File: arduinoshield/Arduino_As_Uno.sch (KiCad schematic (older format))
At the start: 25 parts, among them J1 Conn_01x08, P1 Power, P2 Analog, P3 Digital, P4 Digital, P5 CONN_01X01, P6 CONN_01X01, P7 CONN_01X01, P8 CONN_01X01, U1 MC7815ACTG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

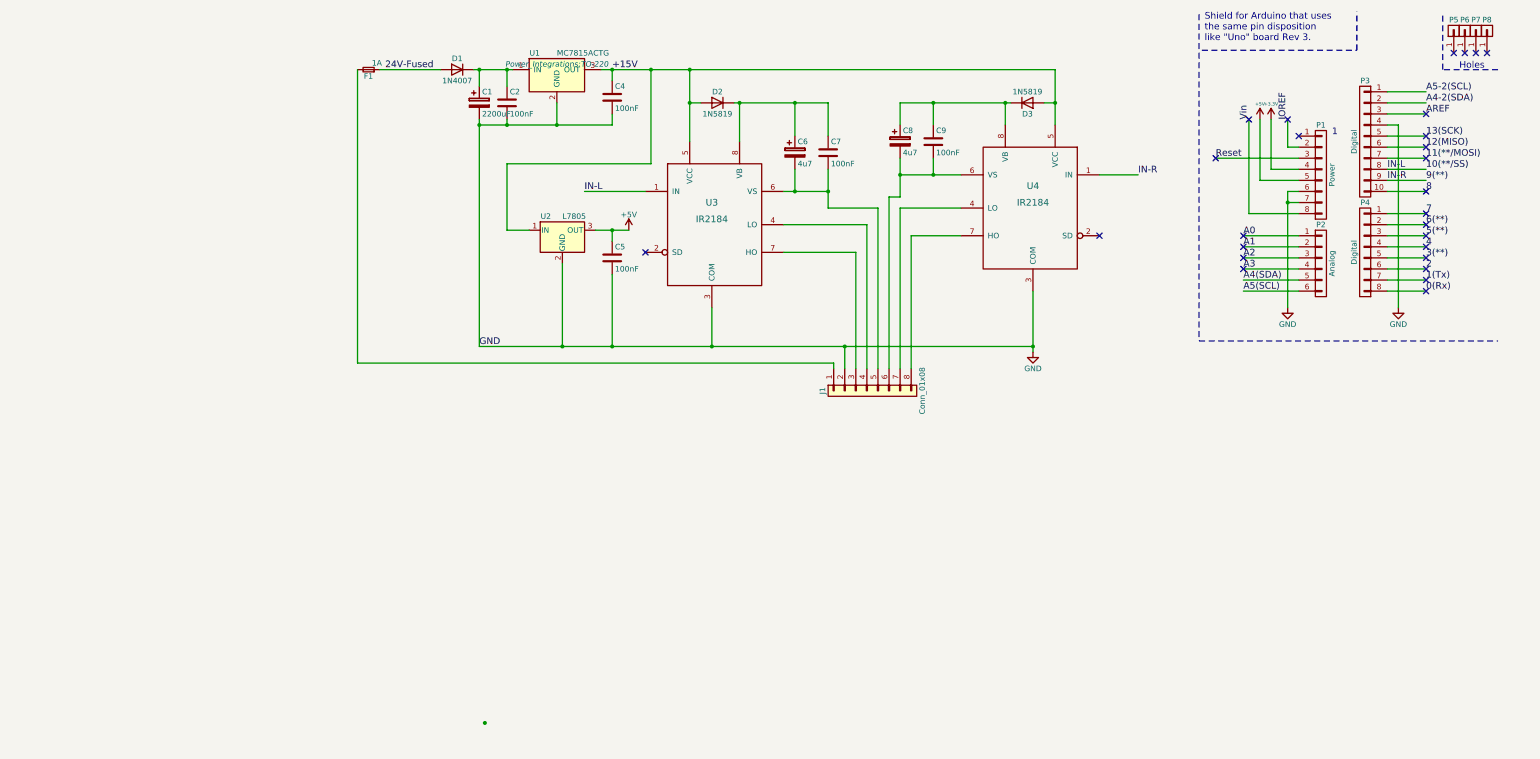
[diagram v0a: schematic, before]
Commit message: redesigned arduino shield for with connectors and smd parts
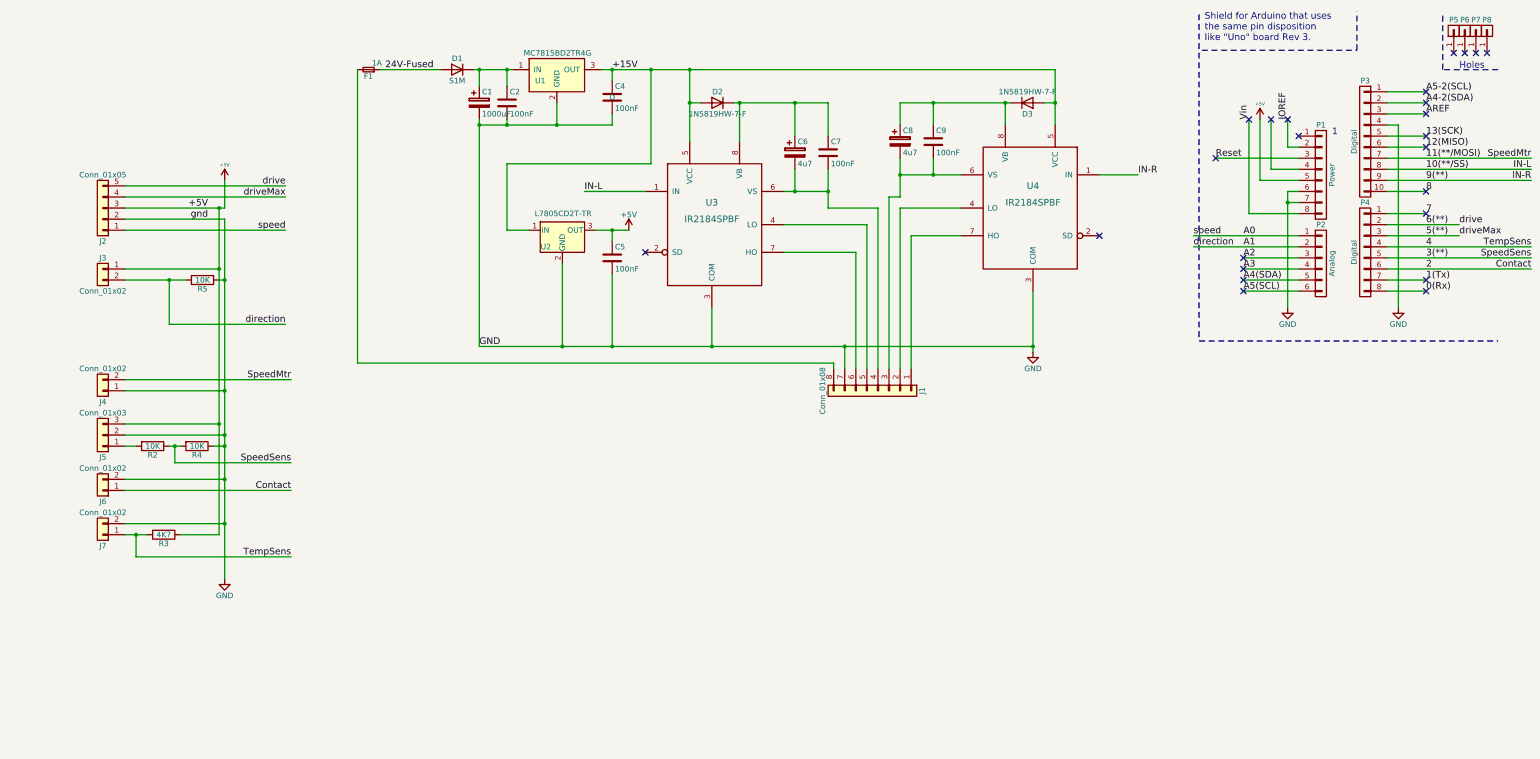
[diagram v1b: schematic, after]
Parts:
- added J2: Conn_01x05, Connectors_JST:JST_XH_B05B-XH-A_05x2.50mm_Straight, symbol Conn_01x05
- added J3, J4, J6, J7: Conn_01x02, Connectors_JST:JST_XH_B02B-XH-A_02x2.50mm_Straight, symbol Conn_01x02
- added J5: Conn_01x03, Connectors_JST:JST_XH_B03B-XH-A_03x2.50mm_Straight, symbol Conn_01x03
- added R2, R4, R5: 10K, Resistors_SMD:R_1206_HandSoldering, symbol R
- added R3: 4K7, Resistors_SMD:R_1206_HandSoldering, symbol R
- C1: value 2200uF -> 1000uF; footprint Capacitors_THT:CP_Radial_D22.0mm_P10.00mm_SnapIn -> Capacitors_THT:CP_Radial_D13.0mm_P5.00mm; Distributor (none) -> RS 215-5663; RS 711-1510 -> (none)
- C2: footprint Capacitors_THT:C_Axial_L3.8mm_D2.6mm_P7.50mm_Horizontal -> Capacitors_SMD:C_1206_HandSoldering; Distributor (none) -> RS 464-6852, Farnell 2760711
- C4, C5, C7, C9: footprint Capacitors_THT:C_Axial_L3.8mm_D2.6mm_P7.50mm_Horizontal -> Capacitors_SMD:C_1206_HandSoldering; Distributor (none) -> RS 464-6852
- D1: value 1N4007 -> S1M; footprint Diodes_THT:D_A-405_P12.70mm_Horizontal -> Diodes_SMD:D_2114; Distributor (none) -> RS 670-8836, Farnell 9843841; Fabrikant (none) -> Fairchild
- D2: value 1N5819 -> 1N5819HW-7-F; footprint Diodes_THT:D_A-405_P12.70mm_Horizontal -> Diodes_SMD:D_SOD-123; Distributor (none) -> RS 708-2197; Fabrikant STMicroelectronics -> (none); RS 486-4460 -> (none)
- D3: value 1N5819 -> 1N5819HW-7-F; footprint Diodes_THT:D_A-405_P12.70mm_Horizontal -> Diodes_SMD:D_SOD-123; Distributor (none) -> RS 708-2197, Farnell 1773475; RS 486-4460 -> (none)
- J1: footprint Connectors_Terminal_Blocks:TerminalBlock_Pheonix_MPT-2.54mm_8pol -> Connectors_JST:JST_XH_B08B-XH-A_08x2.50mm_Straight
- U1: value MC7815ACTG -> MC7815BD2TR4G; footprint Power_Integrations:TO-220 -> TO_SOT_Packages_SMD:ATPAK-2; Distributor (none) -> RS 785-6976, Farnell 2464349; Farnell 2382331 -> (none)
- U2: value L7805 -> L7805CD2T-TR; footprint Power_Integrations:TO-220 -> TO_SOT_Packages_SMD:ATPAK-2; Distributor (none) -> Farnell 1366576; RS 843-1566 -> (none)
- U3, U4: value IR2184 -> IR2184SPBF; footprint Housings_DIP:DIP-8_W7.62mm -> SMD_Packages:SOIC-8-N; Distributor (none) -> Farnell 8639051, RS 784-0265; RS 543-0771 -> (none)
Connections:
- net +5V: now also J2.3 (Pin_3), J3.1 (Pin_1), J5.3 (Pin_3), R3.1
- net 11(**/MOSI): now also J4.2 (Pin_2)
- net 2: now also J6.1 (Pin_1)
- net 3(**): now also R2.1, R4.2
- net 4: now also J7.1 (Pin_1), R3.2
- net 5(**): now also J2.4 (Pin_4)
- net 6(**): now also J2.5 (Pin_5)
- net A0: now also J2.1 (Pin_1)
- net A1: now also J3.2 (Pin_2), R5.2
- net GND: now also J1.7 (Pin_7), J2.2 (Pin_2), J4.1 (Pin_1), J5.2 (Pin_2), J6.2 (Pin_2), J7.2 (Pin_2), R4.1, R5.1; no longer J1.2 (Pin_2)
- net at U3.4 (LO): now also J1.5 (Pin_5); no longer J1.4 (Pin_4)
- net at C6.2, C7.2, U3.6 (VS): now also J1.4 (Pin_4); no longer J1.5 (Pin_5)
- net at U3.7 (HO): now also J1.6 (Pin_6); no longer J1.3 (Pin_3)
- net at U4.4 (LO): now also J1.2 (Pin_2); no longer J1.7 (Pin_7)
- net at C8.2, C9.2, U4.6 (VS): now also J1.3 (Pin_3); no longer J1.6 (Pin_6)
- net at U4.7 (HO): now also J1.1 (Pin_1); no longer J1.8 (Pin_8)
- net at F1.2: now also J1.8 (Pin_8); no longer J1.1 (Pin_1)
- net +3V3: no longer names the net of P1.4 (P4)
- new net: J5.1 (Pin_1), R2.2
- no-connect marks 27 -> 24

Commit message: New controller design
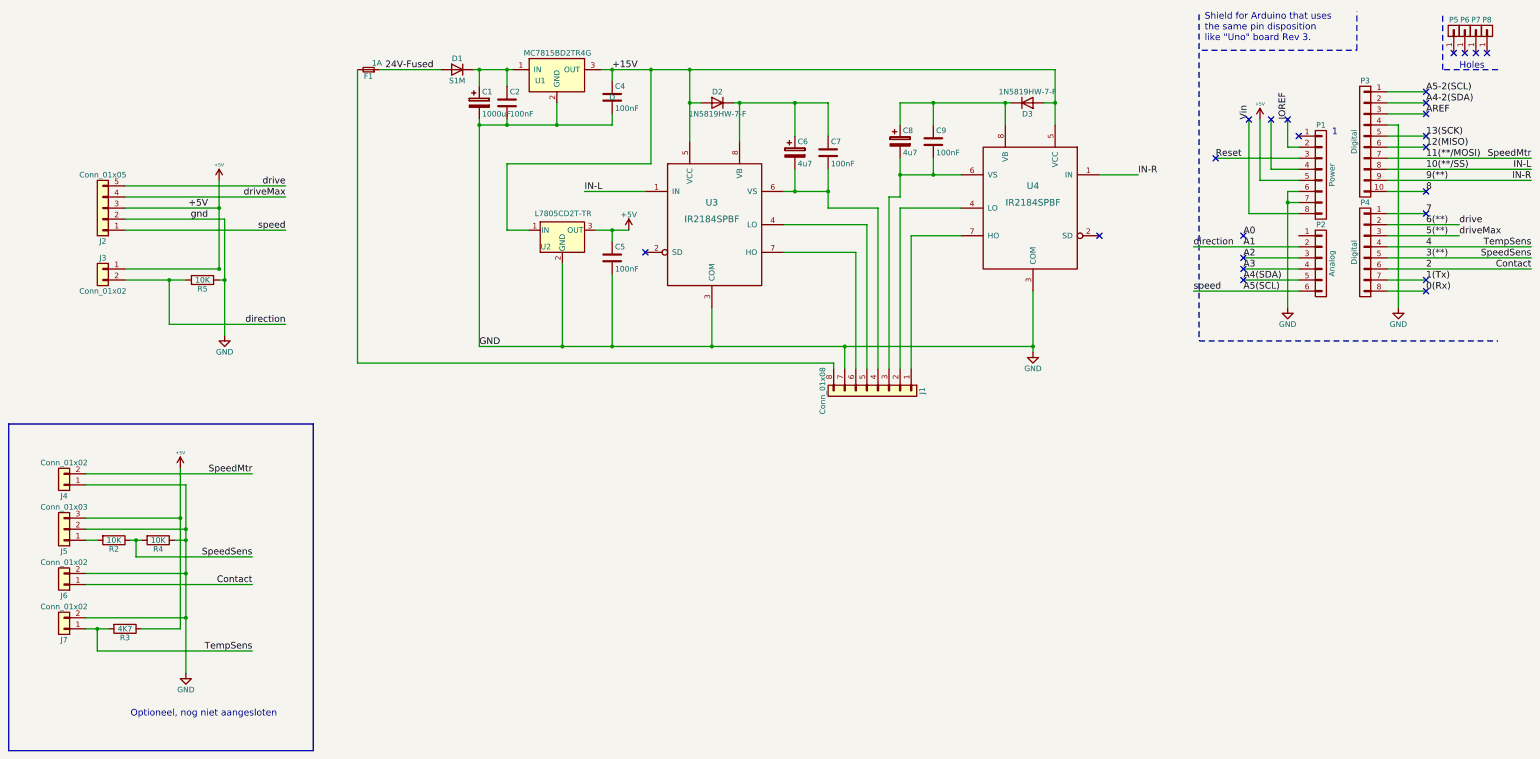
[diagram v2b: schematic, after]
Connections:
- net A0: no longer J2.1 (Pin_1), P2.1 (P1)
- net A5(SCL): now also J2.1 (Pin_1)
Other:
- note added: "Optioneel, nog niet aangesloten"
- moved on the sheet: J4, J5, J6, J7, R2, R3, R4
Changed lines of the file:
@@
 	13150 1900 13150 1450
 Wire Wire Line
-	12450 2500 13400 2500
-Wire Wire Line
 	12450 2600 13400 2600
 Wire Wire Line
@@
 	13400 2900 12900 2900
 Wire Wire Line
-	13400 3000 12900 3000
+	12450 3000 13400 3000
 Wire Wire Line
 	14200 2100 14550 2100
@@
 Wire Wire Line
 	14200 1300 14550 1300
-Wire Wire Line
-	14200 1200 14550 1200
 Wire Wire Line
 	14200 3000 14550 3000
@@
 	2800 2150 4250 2150
 Wire Wire Line
-	2800 2250 3700 2250
-Wire Wire Line
 	2800 2350 3700 2350
 Wire Wire Line
@@
 L +5V #PWR06
 U 1 1 59E67B47
-P 3700 2000
-F 0 "#PWR06" H 3700 1850 50  0001 C CNN
-F 1 "+5V" H 3700 2140 30  0000 C CNN
-F 2 "" H 3700 2000 50  0000 C CNN
-F 3 "" H 3700 2000 50  0000 C CNN
-	1    3700 2000
+P 3650 2000
+F 0 "#PWR06" H 3650 1850 50  0001 C CNN
+F 1 "+5V" H 3650 2140 30  0000 C CNN
+F 2 "" H 3650 2000 50  0000 C CNN
+F 3 "" H 3650 2000 50  0000 C CNN
+	1    3650 2000
 	1    0    0    -1
 $EndComp
-Wire Wire Line
-	3700 2250 3700 2000
-Wire Wire Line
-	3700 2350 3700 5600
-Text Label 12450 2500 0    60   ~ 0
+Text Label 12450 3000 0    60   ~ 0
 speed
 Wire Wire Line
-	2800 2800 3650 2800
-Wire Wire Line
-	3650 2250 3650 5200
+	3650 2800 2800 2800
 Connection ~ 3650 2250
 $Comp
@@
 L Conn_01x02 J4
 U 1 1 59E69F43
-P 2600 3900
-F 0 "J4" H 2600 4000 50  0000 C CNN
-F 1 "Conn_01x02" H 2600 3700 50  0000 C CNN
-F 2 "Connectors_JST:JST_XH_B02B-XH-A_02x2.50mm_Straight" H 2600 3900 50  0001 C CNN
-F 3 "" H 2600 3900 50  0001 C CNN
-	1    2600 3900
+P 2250 4750
+F 0 "J4" H 2250 4850 50  0000 C CNN
+F 1 "Conn_01x02" H 2250 4550 50  0000 C CNN
+F 2 "Connectors_JST:JST_XH_B02B-XH-A_02x2.50mm_Straight" H 2250 4750 50  0001 C CNN
+F 3 "" H 2250 4750 50  0001 C CNN
+	1    2250 4750
 	-1   0    0    1
 $EndComp
 Text Label 15500 1800 2    60   ~ 0
 SpeedMtr
-Text Label 4300 3800 2    60   ~ 0
+Text Label 3950 4650 2    60   ~ 0
 SpeedMtr
 Wire Wire Line
-	3700 3900 2800 3900
+	3350 4750 2450 4750
 $Comp
 L GND #PWR07
 U 1 1 59E6B36E
-P 3700 5600
-F 0 "#PWR07" H 3700 5350 50  0001 C CNN
-F 1 "GND" H 3700 5450 50  0000 C CNN
-F 2 "" H 3700 5600 50  0000 C CNN
-F 3 "" H 3700 5600 50  0000 C CNN
-	1    3700 5600
+P 3350 6450
+F 0 "#PWR07" H 3350 6200 50  0001 C CNN
+F 1 "GND" H 3350 6300 50  0000 C CNN
+F 2 "" H 3350 6450 50  0000 C CNN
+F 3 "" H 3350 6450 50  0000 C CNN
+	1    3350 6450
 	1    0    0    -1
 $EndComp
@@
 L Conn_01x03 J5
 U 1 1 59E6B665
-P 2600 4300
-F 0 "J5" H 2600 4500 50  0000 C CNN
-F 1 "Conn_01x03" H 2600 4100 50  0000 C CNN
-F 2 "Connectors_JST:JST_XH_B03B-XH-A_03x2.50mm_Straight" H 2600 4300 50  0001 C CNN
-F 3 "" H 2600 4300 50  0001 C CNN
-	1    2600 4300
+P 2250 5150
+F 0 "J5" H 2250 5350 50  0000 C CNN
+F 1 "Conn_01x03" H 2250 4950 50  0000 C CNN
+F 2 "Connectors_JST:JST_XH_B03B-XH-A_03x2.50mm_Straight" H 2250 5150 50  0001 C CNN
+F 3 "" H 2250 5150 50  0001 C CNN
+	1    2250 5150
 	-1   0    0    1
 $EndComp
-Connection ~ 3700 3900
-Wire Wire Line
-	3650 4200 2800 4200
+Wire Wire Line
+	3300 5050 2450 5050
 Connection ~ 3650 2800
 $Comp
 L R R2
 U 1 1 59E6BE84
-P 3050 4400
-F 0 "R2" V 3130 4400 50  0000 C CNN
-F 1 "10K" V 3050 4400 50  0000 C CNN
-F 2 "Resistors_SMD:R_1206_HandSoldering" V 2980 4400 50  0001 C CNN
-F 3 "" H 3050 4400 50  0001 C CNN
-F 4 "RS 802-9692" V 3050 4400 60  0001 C CNN "Distributor"
-	1    3050 4400
+P 2700 5250
+F 0 "R2" V 2780 5250 50  0000 C CNN
+F 1 "10K" V 2700 5250 50  0000 C CNN
+F 2 "Resistors_SMD:R_1206_HandSoldering" V 2630 5250 50  0001 C CNN
+F 3 "" H 2700 5250 50  0001 C CNN
+F 4 "RS 802-9692" V 2700 5250 60  0001 C CNN "Distributor"
+	1    2700 5250
 	0    1    1    0
 $EndComp
 Wire Wire Line
-	2800 4300 3700 4300
-Connection ~ 3700 4300
+	2450 5150 3350 5150
+Connection ~ 3350 5150
 $Comp
 L R R4
 U 1 1 59E6C1EF
-P 3450 4400
-F 0 "R4" V 3530 4400 50  0000 C CNN
-F 1 "10K" V 3450 4400 50  0000 C CNN
-F 2 "Resistors_SMD:R_1206_HandSoldering" V 3380 4400 50  0001 C CNN
-F 3 "" H 3450 4400 50  0001 C CNN
-F 4 "RS 802-9692" V 3450 4400 60  0001 C CNN "Distributor"
-	1    3450 4400
+P 3100 5250
+F 0 "R4" V 3180 5250 50  0000 C CNN
+F 1 "10K" V 3100 5250 50  0000 C CNN
+F 2 "Resistors_SMD:R_1206_HandSoldering" V 3030 5250 50  0001 C CNN
+F 3 "" H 3100 5250 50  0001 C CNN
+F 4 "RS 802-9692" V 3100 5250 60  0001 C CNN "Distributor"
+	1    3100 5250
 	0    1    1    0
 $EndComp
 Wire Wire Line
-	2800 4400 2900 4400
-Wire Wire Line
-	3200 4400 3300 4400
-Wire Wire Line
-	3600 4400 3700 4400
-Connection ~ 3700 4400
-Wire Wire Line
-	3250 4400 3250 4550
-Wire Wire Line
-	3250 4550 4300 4550
-Connection ~ 3250 4400
-Text Label 4300 4550 2    60   ~ 0
+	2450 5250 2550 5250
+Wire Wire Line
+	2850 5250 2950 5250
+Wire Wire Line
+	3250 5250 3350 5250
+Connection ~ 3350 5250
+Wire Wire Line
+	2900 5250 2900 5400
+Wire Wire Line
+	2900 5400 3950 5400
+Connection ~ 2900 5250
+Text Label 3950 5400 2    60   ~ 0
 SpeedSens
 Text Label 15500 2700 2    60   ~ 0
@@
 L Conn_01x02 J6
 U 1 1 59E6F50D
-P 2600 4800
-F 0 "J6" H 2600 4900 50  0000 C CNN
-F 1 "Conn_01x02" H 2600 4600 50  0000 C CNN
-F 2 "Connectors_JST:JST_XH_B02B-XH-A_02x2.50mm_Straight" H 2600 4800 50  0001 C CNN
-F 3 "" H 2600 4800 50  0001 C CNN
-	1    2600 4800
+P 2250 5650
+F 0 "J6" H 2250 5750 50  0000 C CNN
+F 1 "Conn_01x02" H 2250 5450 50  0000 C CNN
+F 2 "Connectors_JST:JST_XH_B02B-XH-A_02x2.50mm_Straight" H 2250 5650 50  0001 C CNN
+F 3 "" H 2250 5650 50  0001 C CNN
+	1    2250 5650
 	-1   0    0    1
 $EndComp
 Wire Wire Line
-	2800 4800 4300 4800
-Text Label 4300 4800 2    60   ~ 0
+	2450 5650 3950 5650
+Text Label 3950 5650 2    60   ~ 0
 Contact
 Wire Wire Line
-	2800 4700 3700 4700
-Connection ~ 3700 4700
+	2450 5550 3350 5550
+Connection ~ 3350 5550
 $Comp
 L Conn_01x02 J7
 U 1 1 59E70900
-P 2600 5200
-F 0 "J7" H 2600 5300 50  0000 C CNN
-F 1 "Conn_01x02" H 2600 5000 50  0000 C CNN
-F 2 "Connectors_JST:JST_XH_B02B-XH-A_02x2.50mm_Straight" H 2600 5200 50  0001 C CNN
-F 3 "" H 2600 5200 50  0001 C CNN
-	1    2600 5200
+P 2250 6050
+F 0 "J7" H 2250 6150 50  0000 C CNN
+F 1 "Conn_01x02" H 2250 5850 50  0000 C CNN
+F 2 "Connectors_JST:JST_XH_B02B-XH-A_02x2.50mm_Straight" H 2250 6050 50  0001 C CNN
+F 3 "" H 2250 6050 50  0001 C CNN
+	1    2250 6050
 	-1   0    0    1
 $EndComp
@@
 L R R3
 U 1 1 59E70E33
-P 3150 5200
-F 0 "R3" V 3230 5200 50  0000 C CNN
-F 1 "4K7" V 3150 5200 50  0000 C CNN
-F 2 "Resistors_SMD:R_1206_HandSoldering" V 3080 5200 50  0001 C CNN
-F 3 "" H 3150 5200 50  0001 C CNN
-F 4 "RS 802-9668" V 3150 5200 60  0001 C CNN "Distributor"
-	1    3150 5200
+P 2800 6050
+F 0 "R3" V 2880 6050 50  0000 C CNN
+F 1 "4K7" V 2800 6050 50  0000 C CNN
+F 2 "Resistors_SMD:R_1206_HandSoldering" V 2730 6050 50  0001 C CNN
+F 3 "" H 2800 6050 50  0001 C CNN
+F 4 "RS 802-9668" V 2800 6050 60  0001 C CNN "Distributor"
+	1    2800 6050
 	0    1    1    0
 $EndComp
 Wire Wire Line
-	3650 5200 3300 5200
-Connection ~ 3650 4200
-Wire Wire Line
-	2800 5200 3000 5200
-Wire Wire Line
-	2800 5100 3700 5100
-Connection ~ 3700 5100
-Wire Wire Line
-	2900 5200 2900 5400
-Wire Wire Line
-	2900 5400 4300 5400
-Connection ~ 2900 5200
+	3300 6050 2950 6050
+Wire Wire Line
+	2450 6050 2650 6050
+Wire Wire Line
+	2450 5950 3350 5950
+Connection ~ 3350 5950
+Wire Wire Line
+	2550 6050 2550 6250
+Wire Wire Line
+	2550 6250 3950 6250
+Connection ~ 2550 6050
 Text Label 15500 2600 2    60   ~ 0
 TempSens
-Text Label 4300 5400 2    60   ~ 0
+Text Label 3950 6250 2    60   ~ 0
 TempSens
 Wire Wire Line
-	2800 3800 4300 3800
-NoConn ~ 14550 1200
+	2450 4650 3950 4650
 NoConn ~ 14550 1300
 NoConn ~ 12900 2900
-NoConn ~ 12900 3000
 NoConn ~ 13150 1450
+NoConn ~ 12900 2500
+Wire Wire Line
+	3350 6450 3350 4750
+Wire Wire Line
+	3300 4600 3300 6050
+$Comp
+L +5V #PWR?
+U 1 1 5A16C3FA
+P 3300 4600
+F 0 "#PWR?" H 3300 4450 50  0001 C CNN
+F 1 "+5V" H 3300 4740 30  0000 C CNN
+F 2 "" H 3300 4600 50  0000 C CNN
+F 3 "" H 3300 4600 50  0000 C CNN
+	1    3300 4600
+	1    0    0    -1
+$EndComp
+Connection ~ 3300 5050
+$Comp
+L GND #PWR?
+U 1 1 5A16C846
+P 3700 3400
+F 0 "#PWR?" H 3700 3150 50  0001 C CNN
+F 1 "GND" H 3700 3250 50  0000 C CNN
+F 2 "" H 3700 3400 50  0000 C CNN
+F 3 "" H 3700 3400 50  0000 C CNN
+	1    3700 3400
+	1    0    0    -1
+$EndComp
+Wire Wire Line
+	3650 2000 3650 2800
+Wire Wire Line
+	3700 2350 3700 3400
+Wire Wire Line
+	2800 2250 3650 2250
+Wire Bus Line
+	1750 4200 4500 4200
+Wire Bus Line
+	4500 4200 4500 7150
+Wire Bus Line
+	4500 7150 1750 7150
+Wire Bus Line
+	1750 7150 1750 4200
+Text Notes 2850 6850 0    60   ~ 0
+Optioneel, nog niet aangesloten
+Wire Wire Line
+	14200 1200 14550 1200
+NoConn ~ 14550 1200
 $EndSCHEMATC
